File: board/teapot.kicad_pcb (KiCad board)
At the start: 2 copper layers, 50 x 50 mm, 9 parts, among them P1 BATT, P2 SMA, Q1 TEPT4400, U1 TLV61225, U3 RFM69W, U4 STM32L052K8, U5 HTU21D, U6 MS5637, U7 SWD

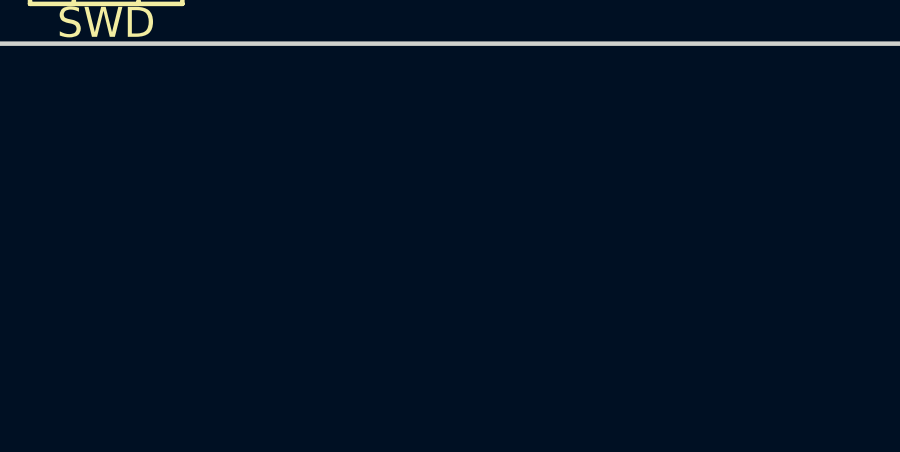
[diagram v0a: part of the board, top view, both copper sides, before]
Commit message: Added USB LDO.  Resolves #9
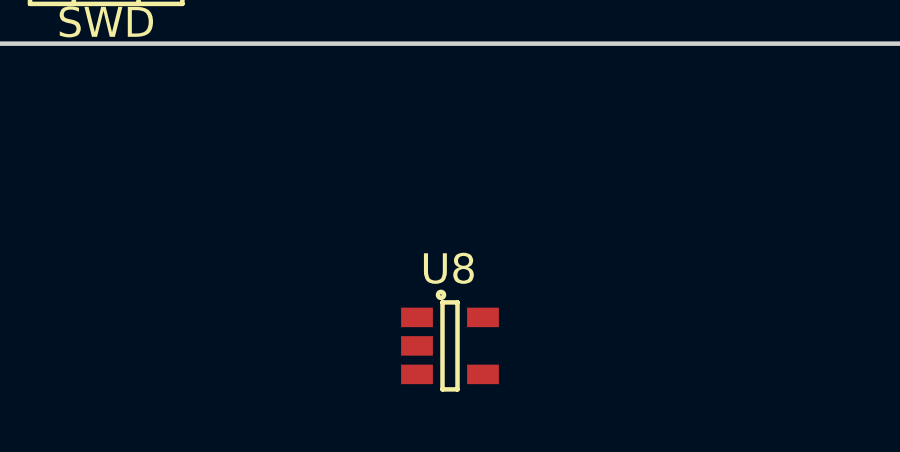
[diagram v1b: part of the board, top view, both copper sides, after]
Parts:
- added U8: TPS79333DBVR, TO_SOT_Packages_SMD:SOT-23-5, F.Cu at (127.0, 148.1)
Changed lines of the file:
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@@
 (kicad_pcb (version 4) (host pcbnew 4.0.1-3.201512150931+6195~38~ubuntu14.04.1-stable)
   (general
-    (links 31)
-    (no_connects 31)
+    (links 34)
+    (no_connects 34)
     (area 101.924999 87.924999 152.075001 138.075001)
     (thickness 1.6)
@@
     (tracks 0)
     (zones 0)
-    (modules 9)
-    (nets 10)
+    (modules 10)
+    (nets 11)
   )
   (page A4)
@@
   (net 8 /I2C_SDA)
   (net 9 "Net-(P2-Pad1)")
+  (net 10 +5V)
   (net_class Default "This is the default net class."
     (clearance 0.2)
@@
     (uvia_drill 0.1)
     (add_net +3V3)
+    (add_net +5V)
     (add_net /I2C_SCK)
     (add_net /I2C_SDA)
@@
       (net 3 GND) (zone_connect 1) (thermal_width 0.5) (thermal_gap 0.2))
   )
+  (module TO_SOT_Packages_SMD:SOT-23-5 (layer F.Cu)
+    (at 127 148.075001)
+    (descr "5-pin SOT23 package")
+    (tags SOT-23-5)
+    (attr smd)
+    (fp_text reference U8 (at -0.05 -2.55) (layer F.SilkS)
+      (effects (font (size 1 1) (thickness 0.15)))
+    )
+    (fp_text value TPS79333DBVR (at -0.05 2.35) (layer F.Fab)
+      (effects (font (size 1 1) (thickness 0.15)))
+    )
+    (fp_line (start -1.8 -1.6) (end 1.8 -1.6) (layer F.CrtYd) (width 0.05))
+    (fp_line (start 1.8 -1.6) (end 1.8 1.6) (layer F.CrtYd) (width 0.05))
+    (fp_line (start 1.8 1.6) (end -1.8 1.6) (layer F.CrtYd) (width 0.05))
+    (fp_line (start -1.8 1.6) (end -1.8 -1.6) (layer F.CrtYd) (width 0.05))
+    (fp_circle (center -0.3 -1.7) (end -0.2 -1.7) (layer F.SilkS) (width 0.15))
+    (fp_line (start 0.25 -1.45) (end -0.25 -1.45) (layer F.SilkS) (width 0.15))
+    (fp_line (start 0.25 1.45) (end 0.25 -1.45) (layer F.SilkS) (width 0.15))
+    (fp_line (start -0.25 1.45) (end 0.25 1.45) (layer F.SilkS) (width 0.15))
+    (fp_line (start -0.25 -1.45) (end -0.25 1.45) (layer F.SilkS) (width 0.15))
+    (pad 1 smd rect (at -1.1 -0.95) (size 1.06 0.65) (layers F.Cu F.Paste F.Mask)
+      (net 10 +5V))
+    (pad 2 smd rect (at -1.1 0) (size 1.06 0.65) (layers F.Cu F.Paste F.Mask)
+      (net 3 GND))
+    (pad 3 smd rect (at -1.1 0.95) (size 1.06 0.65) (layers F.Cu F.Paste F.Mask)
+      (net 10 +5V))
+    (pad 4 smd rect (at 1.1 0.95) (size 1.06 0.65) (layers F.Cu F.Paste F.Mask))
+    (pad 5 smd rect (at 1.1 -0.95) (size 1.06 0.65) (layers F.Cu F.Paste F.Mask)
+      (net 1 +3V3))
+    (model TO_SOT_Packages_SMD.3dshapes/SOT-23-5.wrl
+      (at (xyz 0 0 0))
+      (scale (xyz 1 1 1))
+      (rotate (xyz 0 0 0))
+    )
+  )
   (gr_line (start 102 97.5) (end 102 128.5) (angle 90) (layer Edge.Cuts) (width 0.15))

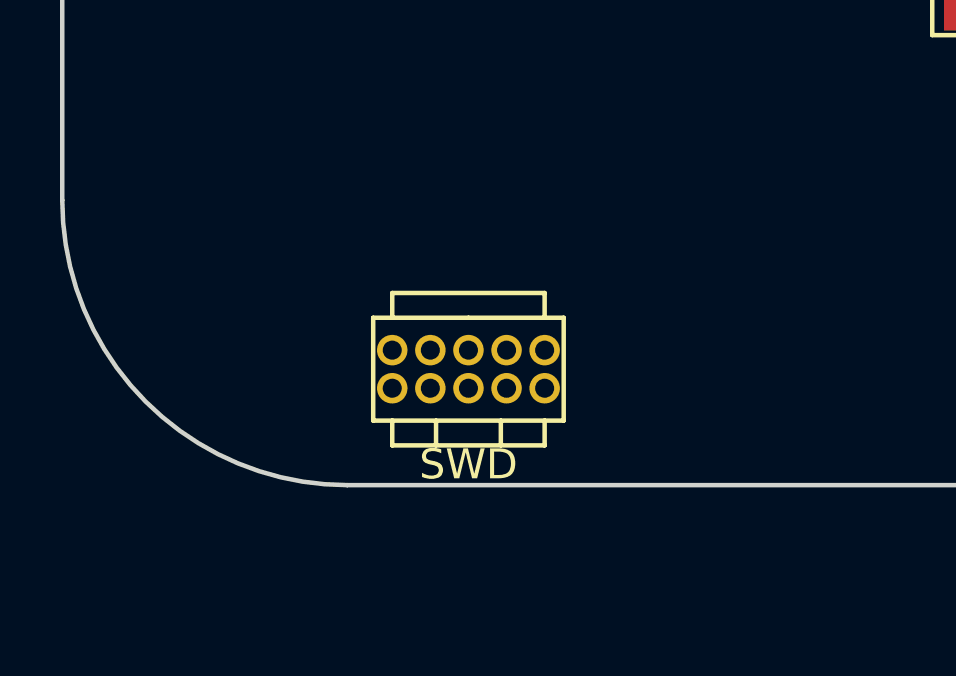
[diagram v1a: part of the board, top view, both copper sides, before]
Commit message: Added microusb footprint, resolves #6
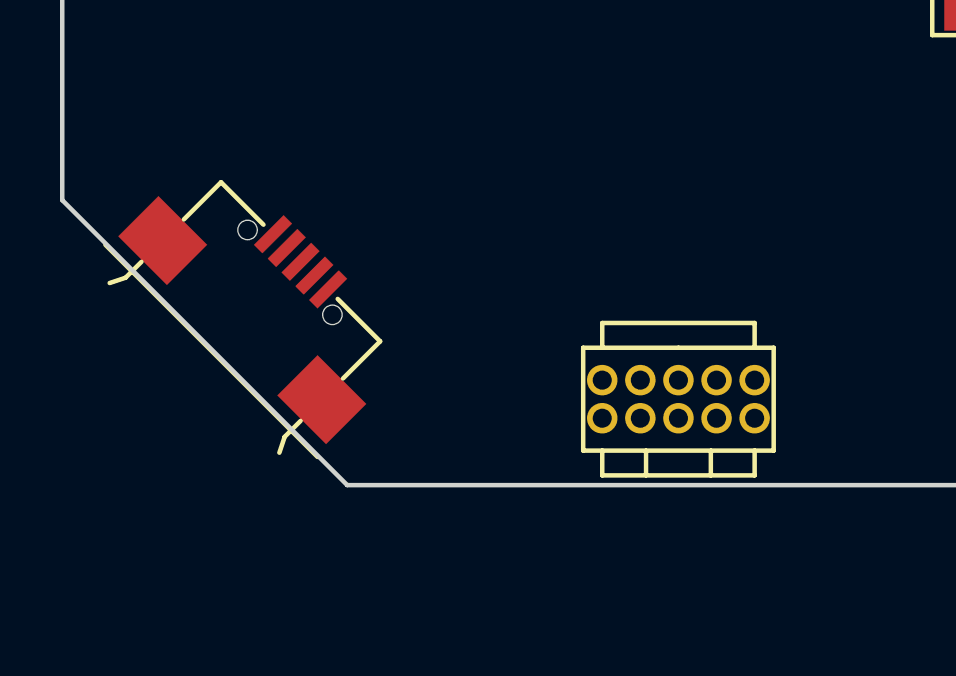
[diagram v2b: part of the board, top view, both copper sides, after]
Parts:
- added U2: microusb-b, footprints:USB3065, F.Cu at (108.0, 132.5)
- moved U7 7.07 mm to (120.0, 134.5)
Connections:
- U4 pad 21: (no net) -> /USB_DM
- U4 pad 22: (no net) -> /USB_DP
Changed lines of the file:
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@@
 (kicad_pcb (version 4) (host pcbnew 4.0.1-3.201512150931+6195~38~ubuntu14.04.1-stable)
   (general
-    (links 34)
-    (no_connects 34)
+    (links 38)
+    (no_connects 38)
     (area 101.924999 87.924999 152.075001 138.075001)
     (thickness 1.6)
@@
     (tracks 0)
     (zones 0)
-    (modules 10)
-    (nets 11)
+    (modules 11)
+    (nets 13)
   )
   (page A4)
@@
   (net 9 "Net-(P2-Pad1)")
   (net 10 +5V)
+  (net 11 /USB_DM)
+  (net 12 /USB_DP)
   (net_class Default "This is the default net class."
     (clearance 0.2)
@@
     (add_net /SWCLK)
     (add_net /SWDIO)
+    (add_net /USB_DM)
+    (add_net /USB_DP)
     (add_net /nRST)
     (add_net GND)
@@
     (pad 19 smd rect (at 2.35 0.75) (size 0.6 0.3) (layers F.Cu F.Paste F.Mask))
     (pad 20 smd rect (at 2.35 0.25) (size 0.6 0.3) (layers F.Cu F.Paste F.Mask))
-    (pad 21 smd rect (at 2.35 -0.25) (size 0.6 0.3) (layers F.Cu F.Paste F.Mask))
-    (pad 22 smd rect (at 2.35 -0.75) (size 0.6 0.3) (layers F.Cu F.Paste F.Mask))
+    (pad 21 smd rect (at 2.35 -0.25) (size 0.6 0.3) (layers F.Cu F.Paste F.Mask)
+      (net 11 /USB_DM))
+    (pad 22 smd rect (at 2.35 -0.75) (size 0.6 0.3) (layers F.Cu F.Paste F.Mask)
+      (net 12 /USB_DP))
     (pad 23 smd rect (at 2.35 -1.25) (size 0.6 0.3) (layers F.Cu F.Paste F.Mask)
       (net 5 /SWDIO))
@@
   )
   (module footprints:SWD (layer F.Cu)
-    (at 113 133.5)
+    (at 120 134.5)
     (fp_text reference U7 (at 2.5 -2.9) (layer F.SilkS) hide
       (effects (font (size 1 1) (thickness 0.15)))
     )
-    (fp_text value SWD (at 2.54 3.81) (layer F.SilkS)
+    (fp_text value SWD (at 2.54 3.81) (layer F.SilkS) hide
       (effects (font (size 1 1) (thickness 0.15)))
     )
@@
     )
   )
+  (module footprints:USB3065 (layer F.Cu)
+    (at 108 132.5 315)
+    (fp_text reference U2 (at -5.656854 -2.12132 315) (layer F.SilkS) hide
+      (effects (font (size 1.5 1.5) (thickness 0.15)))
+    )
+    (fp_text value microusb-b (at 0 -4.75 315) (layer F.Fab) hide
+      (effects (font (size 1.5 1.5) (thickness 0.15)))
+    )
+    (fp_line (start 3.75 1) (end 3.75 1.75) (layer F.SilkS) (width 0.15))
+    (fp_line (start 3.75 1.75) (end 4 2.25) (layer F.SilkS) (width 0.15))
+    (fp_line (start -3.75 1) (end -3.75 1.75) (layer F.SilkS) (width 0.15))
+    (fp_line (start -3.75 1.75) (end -4 2.25) (layer F.SilkS) (width 0.15))
+    (fp_line (start 1.75 -2.75) (end 3.75 -2.75) (layer F.SilkS) (width 0.15))
+    (fp_line (start 3.75 -2.75) (end 3.75 -1) (layer F.SilkS) (width 0.15))
+    (fp_line (start -3.75 -1) (end -3.75 -2.75) (layer F.SilkS) (width 0.15))
+    (fp_line (start -3.75 -2.75) (end -1.75 -2.75) (layer F.SilkS) (width 0.15))
+    (fp_line (start -5 1.45) (end 5 1.45) (layer F.SilkS) (width 0.15))
+    (pad 1 smd rect (at -1.3 -2.75 315) (size 0.4 1.4) (layers F.Cu F.Paste F.Mask)
+      (net 10 +5V))
+    (pad 2 smd rect (at -0.65 -2.75 315) (size 0.4 1.4) (layers F.Cu F.Paste F.Mask)
+      (net 11 /USB_DM))
+    (pad 3 smd rect (at 0 -2.75 315) (size 0.4 1.4) (layers F.Cu F.Paste F.Mask)
+      (net 12 /USB_DP))
+    (pad 4 smd rect (at 0.65 -2.75 315) (size 0.4 1.4) (layers F.Cu F.Paste F.Mask))
+    (pad 5 smd rect (at 1.3 -2.75 315) (size 0.4 1.4) (layers F.Cu F.Paste F.Mask)
+      (net 3 GND))
+    (pad "" np_thru_hole circle (at -2 -2.25 315) (size 0.65 0.65) (drill 0.65) (layers *.Cu *.Mask F.SilkS))
+    (pad "" np_thru_hole circle (at 2 -2.25 315) (size 0.65 0.65) (drill 0.65) (layers *.Cu *.Mask F.SilkS))
+    (pad 6 smd rect (at -3.75 0 315) (size 2.3 1.9) (layers F.Cu F.Paste F.Mask))
+    (pad 7 smd rect (at 3.75 0 315) (size 2.3 1.9) (layers F.Cu F.Paste F.Mask))
+  )
+  (gr_line (start 102 128.5) (end 111.5 138) (angle 90) (layer Edge.Cuts) (width 0.15))
   (gr_line (start 102 97.5) (end 102 128.5) (angle 90) (layer Edge.Cuts) (width 0.15))
-  (gr_arc (start 111.5 128.5) (end 111.5 138) (angle 90) (layer Edge.Cuts) (width 0.15))
   (gr_line (start 111.5 138) (end 142.5 138) (angle 90) (layer Edge.Cuts) (width 0.15))
   (gr_line (start 152 97.5) (end 152 128.5) (angle 90) (layer Edge.Cuts) (width 0.15))

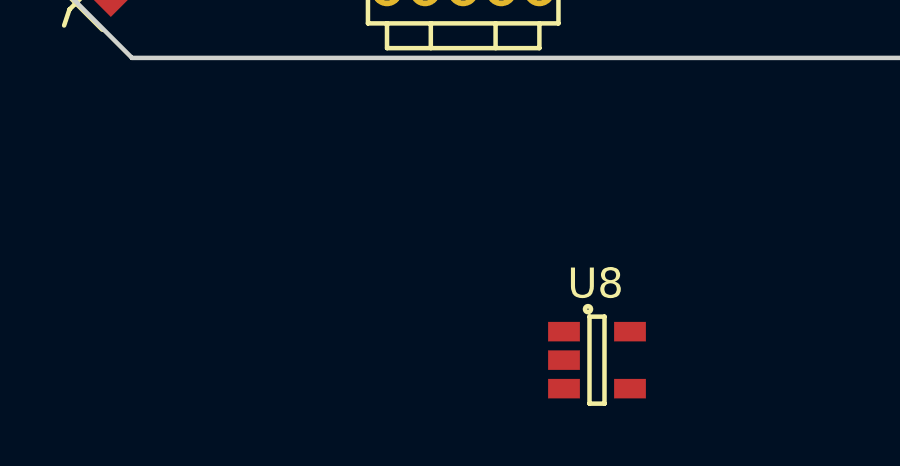
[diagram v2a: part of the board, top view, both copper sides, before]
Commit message: Finished speccings parts and footprints.
Resolves #3
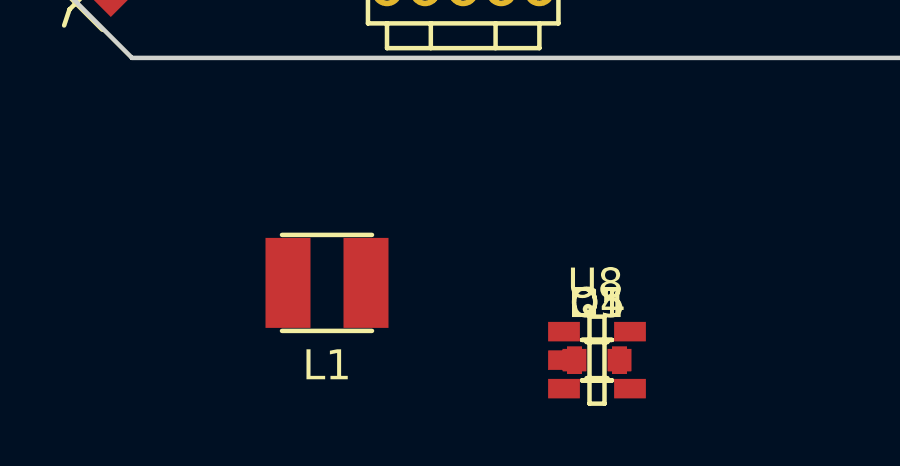
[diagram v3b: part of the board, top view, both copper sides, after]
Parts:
- added C1: 10u, Capacitors_SMD:C_0603, F.Cu at (127.0, 148.1)
- added D4, D5: TVS_small, Resistors_SMD:R_0603, F.Cu at (127.0, 148.1)
- added L1: 4u7, footprints:Inductor_1212, F.Cu at (118.0, 145.5)
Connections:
- U1 pad 5: (no net) -> Net-(L1-Pad2)
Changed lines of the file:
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@@
 (kicad_pcb (version 4) (host pcbnew 4.0.1-3.201512150931+6195~38~ubuntu14.04.1-stable)
   (general
-    (links 38)
-    (no_connects 38)
+    (links 46)
+    (no_connects 42)
     (area 101.924999 87.924999 152.075001 138.075001)
     (thickness 1.6)
@@
     (tracks 0)
     (zones 0)
-    (modules 11)
-    (nets 13)
+    (modules 15)
+    (nets 14)
   )
   (page A4)
@@
   (net 7 /I2C_SCK)
   (net 8 /I2C_SDA)
-  (net 9 "Net-(P2-Pad1)")
-  (net 10 +5V)
-  (net 11 /USB_DM)
-  (net 12 /USB_DP)
+  (net 9 +5V)
+  (net 10 /USB_DM)
+  (net 11 /USB_DP)
+  (net 12 "Net-(D5-Pad2)")
+  (net 13 "Net-(L1-Pad2)")
   (net_class Default "This is the default net class."
     (clearance 0.2)
@@
     (add_net GND)
     (add_net "Net-(C1-Pad1)")
-    (add_net "Net-(P2-Pad1)")
+    (add_net "Net-(D5-Pad2)")
+    (add_net "Net-(L1-Pad2)")
   )
   (module footprints:AA_holder (layer B.Cu)
@@
     (pad 1 smd rect (at -0.65 -1.1) (size 0.4 0.9) (layers F.Cu F.Paste F.Mask)
       (net 2 "Net-(C1-Pad1)"))
-    (pad 5 smd rect (at 0 -1.1) (size 0.4 0.9) (layers F.Cu F.Paste F.Mask))
+    (pad 5 smd rect (at 0 -1.1) (size 0.4 0.9) (layers F.Cu F.Paste F.Mask)
+      (net 13 "Net-(L1-Pad2)"))
     (pad 4 smd rect (at 0.65 -1.1) (size 0.4 0.9) (layers F.Cu F.Paste F.Mask)
       (net 1 +3V3))
@@
       (net 1 +3V3))
     (pad 10 smd rect (at 8.85 5 90) (size 2 1.2) (layers F.Cu F.Paste F.Mask)
-      (net 9 "Net-(P2-Pad1)"))
+      (net 12 "Net-(D5-Pad2)"))
     (pad 11 smd rect (at 8.85 3 90) (size 2 1.2) (layers F.Cu F.Paste F.Mask)
       (net 3 GND))
@@
     (pad 20 smd rect (at 2.35 0.25) (size 0.6 0.3) (layers F.Cu F.Paste F.Mask))
     (pad 21 smd rect (at 2.35 -0.25) (size 0.6 0.3) (layers F.Cu F.Paste F.Mask)
-      (net 11 /USB_DM))
+      (net 10 /USB_DM))
     (pad 22 smd rect (at 2.35 -0.75) (size 0.6 0.3) (layers F.Cu F.Paste F.Mask)
-      (net 12 /USB_DP))
+      (net 11 /USB_DP))
     (pad 23 smd rect (at 2.35 -1.25) (size 0.6 0.3) (layers F.Cu F.Paste F.Mask)
       (net 5 /SWDIO))
@@
     (fp_line (start -3.1 -2.4) (end -1.2 -2.4) (layer F.SilkS) (width 0.15))
     (pad 1 smd rect (at 0 0 315) (size 2.286 5.08) (layers F.Cu F.Mask)
-      (net 9 "Net-(P2-Pad1)") (clearance 0.2) (zone_connect 2))
+      (net 12 "Net-(D5-Pad2)") (clearance 0.2) (zone_connect 2))
     (pad 2 smd rect (at -4.3815 0 315) (size 2.413 5.08) (layers F.Cu F.Mask)
       (net 3 GND) (zone_connect 1) (thermal_width 0.5) (thermal_gap 0.2))
@@
     (fp_line (start -0.25 -1.45) (end -0.25 1.45) (layer F.SilkS) (width 0.15))
     (pad 1 smd rect (at -1.1 -0.95) (size 1.06 0.65) (layers F.Cu F.Paste F.Mask)
-      (net 10 +5V))
+      (net 9 +5V))
     (pad 2 smd rect (at -1.1 0) (size 1.06 0.65) (layers F.Cu F.Paste F.Mask)
       (net 3 GND))
     (pad 3 smd rect (at -1.1 0.95) (size 1.06 0.65) (layers F.Cu F.Paste F.Mask)
-      (net 10 +5V))
+      (net 9 +5V))
     (pad 4 smd rect (at 1.1 0.95) (size 1.06 0.65) (layers F.Cu F.Paste F.Mask))
     (pad 5 smd rect (at 1.1 -0.95) (size 1.06 0.65) (layers F.Cu F.Paste F.Mask)
@@
     (fp_line (start -5 1.45) (end 5 1.45) (layer F.SilkS) (width 0.15))
     (pad 1 smd rect (at -1.3 -2.75 315) (size 0.4 1.4) (layers F.Cu F.Paste F.Mask)
-      (net 10 +5V))
+      (net 9 +5V))
     (pad 2 smd rect (at -0.65 -2.75 315) (size 0.4 1.4) (layers F.Cu F.Paste F.Mask)
-      (net 11 /USB_DM))
+      (net 10 /USB_DM))
     (pad 3 smd rect (at 0 -2.75 315) (size 0.4 1.4) (layers F.Cu F.Paste F.Mask)
-      (net 12 /USB_DP))
+      (net 11 /USB_DP))
     (pad 4 smd rect (at 0.65 -2.75 315) (size 0.4 1.4) (layers F.Cu F.Paste F.Mask))
     (pad 5 smd rect (at 1.3 -2.75 315) (size 0.4 1.4) (layers F.Cu F.Paste F.Mask)
@@
     (pad 7 smd rect (at 3.75 0 315) (size 2.3 1.9) (layers F.Cu F.Paste F.Mask))
   )
+  (module Capacitors_SMD:C_0603 (layer F.Cu)
+    (at 127 148.075001)
+    (descr "Capacitor SMD 0603, reflow soldering, AVX (see smccp.pdf)")
+    (tags "capacitor 0603")
+    (attr smd)
+    (fp_text reference C1 (at 0 -1.9) (layer F.SilkS)
+      (effects (font (size 1 1) (thickness 0.15)))
+    )
+    (fp_text value 10u (at 0 1.9) (layer F.Fab)
+      (effects (font (size 1 1) (thickness 0.15)))
+    )
+    (fp_line (start -1.45 -0.75) (end 1.45 -0.75) (layer F.CrtYd) (width 0.05))
+    (fp_line (start -1.45 0.75) (end 1.45 0.75) (layer F.CrtYd) (width 0.05))
+    (fp_line (start -1.45 -0.75) (end -1.45 0.75) (layer F.CrtYd) (width 0.05))
+    (fp_line (start 1.45 -0.75) (end 1.45 0.75) (layer F.CrtYd) (width 0.05))
+    (fp_line (start -0.35 -0.6) (end 0.35 -0.6) (layer F.SilkS) (width 0.15))
+    (fp_line (start 0.35 0.6) (end -0.35 0.6) (layer F.SilkS) (width 0.15))
+    (pad 1 smd rect (at -0.75 0) (size 0.8 0.75) (layers F.Cu F.Paste F.Mask)
+      (net 2 "Net-(C1-Pad1)"))
+    (pad 2 smd rect (at 0.75 0) (size 0.8 0.75) (layers F.Cu F.Paste F.Mask)
+      (net 3 GND))
+    (model Capacitors_SMD.3dshapes/C_0603.wrl
+      (at (xyz 0 0 0))
+      (scale (xyz 1 1 1))
+      (rotate (xyz 0 0 0))
+    )
+  )
+  (module Resistors_SMD:R_0603 (layer F.Cu)
+    (at 127 148.075001)
+    (descr "Resistor SMD 0603, reflow soldering, Vishay (see dcrcw.pdf)")
+    (tags "resistor 0603")
+    (attr smd)
+    (fp_text reference D4 (at 0 -1.9) (layer F.SilkS)
+      (effects (font (size 1 1) (thickness 0.15)))
+    )
+    (fp_text value TVS_small (at 0 1.9) (layer F.Fab)
+      (effects (font (size 1 1) (thickness 0.15)))
+    )
+    (fp_line (start -1.3 -0.8) (end 1.3 -0.8) (layer F.CrtYd) (width 0.05))
+    (fp_line (start -1.3 0.8) (end 1.3 0.8) (layer F.CrtYd) (width 0.05))
+    (fp_line (start -1.3 -0.8) (end -1.3 0.8) (layer F.CrtYd) (width 0.05))
+    (fp_line (start 1.3 -0.8) (end 1.3 0.8) (layer F.CrtYd) (width 0.05))
+    (fp_line (start 0.5 0.675) (end -0.5 0.675) (layer F.SilkS) (width 0.15))
+    (fp_line (start -0.5 -0.675) (end 0.5 -0.675) (layer F.SilkS) (width 0.15))
+    (pad 1 smd rect (at -0.75 0) (size 0.5 0.9) (layers F.Cu F.Paste F.Mask)
+      (net 2 "Net-(C1-Pad1)"))
+    (pad 2 smd rect (at 0.75 0) (size 0.5 0.9) (layers F.Cu F.Paste F.Mask)
+      (net 3 GND))
+    (model Resistors_SMD.3dshapes/R_0603.wrl
+      (at (xyz 0 0 0))
+      (scale (xyz 1 1 1))
+      (rotate (xyz 0 0 0))
+    )
+  )
+  (module Resistors_SMD:R_0603 (layer F.Cu)
+    (at 127 148.075001)
+    (descr "Resistor SMD 0603, reflow soldering, Vishay (see dcrcw.pdf)")
+    (tags "resistor 0603")
+    (attr smd)
+    (fp_text reference D5 (at 0 -1.9) (layer F.SilkS)
+      (effects (font (size 1 1) (thickness 0.15)))
+    )
+    (fp_text value TVS_small (at 0 1.9) (layer F.Fab)
+      (effects (font (size 1 1) (thickness 0.15)))
+    )
+    (fp_line (start -1.3 -0.8) (end 1.3 -0.8) (layer F.CrtYd) (width 0.05))
+    (fp_line (start -1.3 0.8) (end 1.3 0.8) (layer F.CrtYd) (width 0.05))
+    (fp_line (start -1.3 -0.8) (end -1.3 0.8) (layer F.CrtYd) (width 0.05))
+    (fp_line (start 1.3 -0.8) (end 1.3 0.8) (layer F.CrtYd) (width 0.05))
+    (fp_line (start 0.5 0.675) (end -0.5 0.675) (layer F.SilkS) (width 0.15))
+    (fp_line (start -0.5 -0.675) (end 0.5 -0.675) (layer F.SilkS) (width 0.15))
+    (pad 1 smd rect (at -0.75 0) (size 0.5 0.9) (layers F.Cu F.Paste F.Mask)
+      (net 3 GND))
+    (pad 2 smd rect (at 0.75 0) (size 0.5 0.9) (layers F.Cu F.Paste F.Mask)
+      (net 12 "Net-(D5-Pad2)"))
+    (model Resistors_SMD.3dshapes/R_0603.wrl
+      (at (xyz 0 0 0))
+      (scale (xyz 1 1 1))
+      (rotate (xyz 0 0 0))
+    )
+  )
+  (module footprints:Inductor_1212 (layer F.Cu)
+    (at 118 145.5)
+    (attr smd)
+    (fp_text reference L1 (at 0 2.75) (layer F.SilkS)
+      (effects (font (size 1 1) (thickness 0.15)))
+    )
+    (fp_text value 4u7 (at 0 -2.75) (layer F.Fab)
+      (effects (font (size 1 1) (thickness 0.15)))
+    )
+    (fp_line (start 1.5 1.6) (end -1.5 1.6) (layer F.SilkS) (width 0.15))
+    (fp_line (start -1.5 -1.6) (end 1.5 -1.6) (layer F.SilkS) (width 0.15))
+    (pad 1 smd rect (at -1.3 0) (size 1.5 3) (layers F.Cu F.Paste F.Mask)
+      (net 2 "Net-(C1-Pad1)"))
+    (pad 2 smd rect (at 1.3 0) (size 1.5 3) (layers F.Cu F.Paste F.Mask)
+      (net 13 "Net-(L1-Pad2)"))
+  )
   (gr_line (start 102 128.5) (end 111.5 138) (angle 90) (layer Edge.Cuts) (width 0.15))
